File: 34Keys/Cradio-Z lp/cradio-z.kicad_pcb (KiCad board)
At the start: 2 copper layers, 114.1 x 83.1 mm, 22 parts, among them J1 MJ-4PP-9, SW10 SW_PUSH, SW11 SW_PUSH, SW12 SW_PUSH, SW14 SW_PUSH, SW15 SW_PUSH, SW16 SW_PUSH, SW17 SW_PUSH, SW18 SW_PUSH, SW2 SW_PUSH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

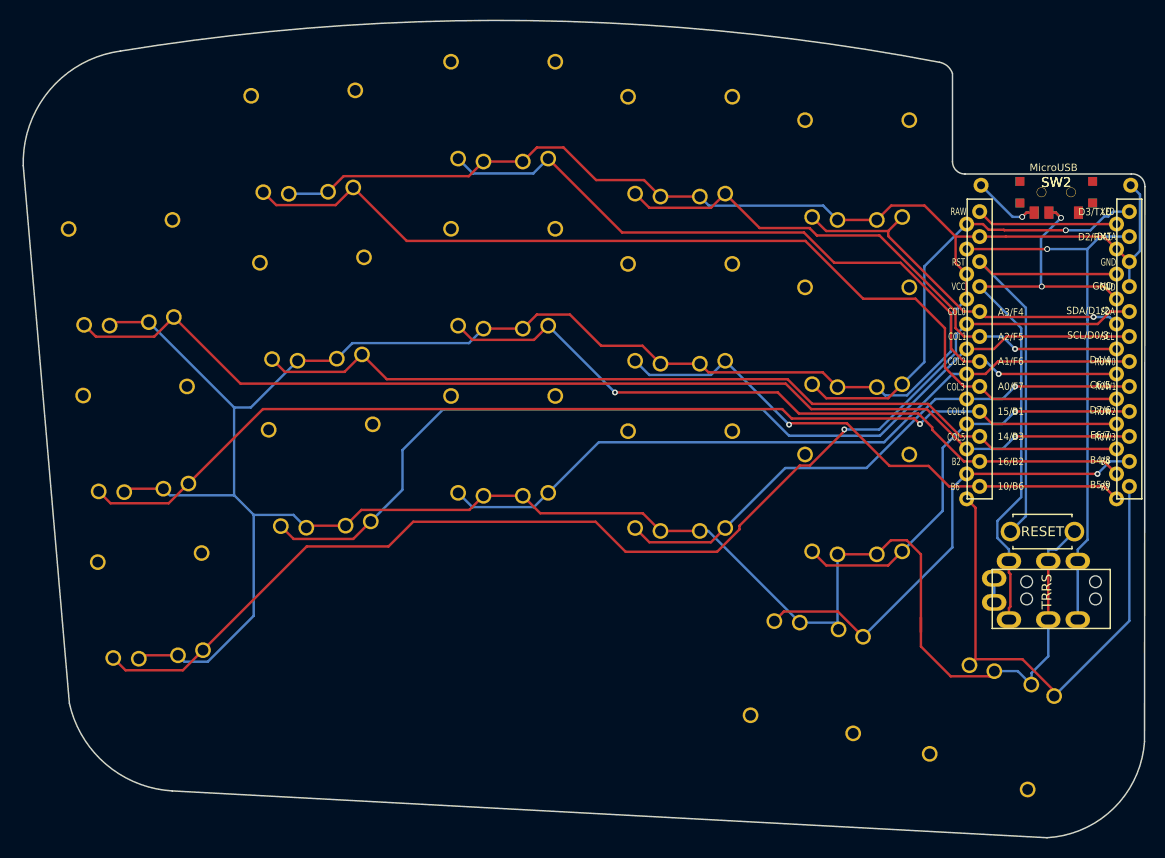
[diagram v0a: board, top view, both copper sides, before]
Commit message: delete somome bits that were really bad or superceded
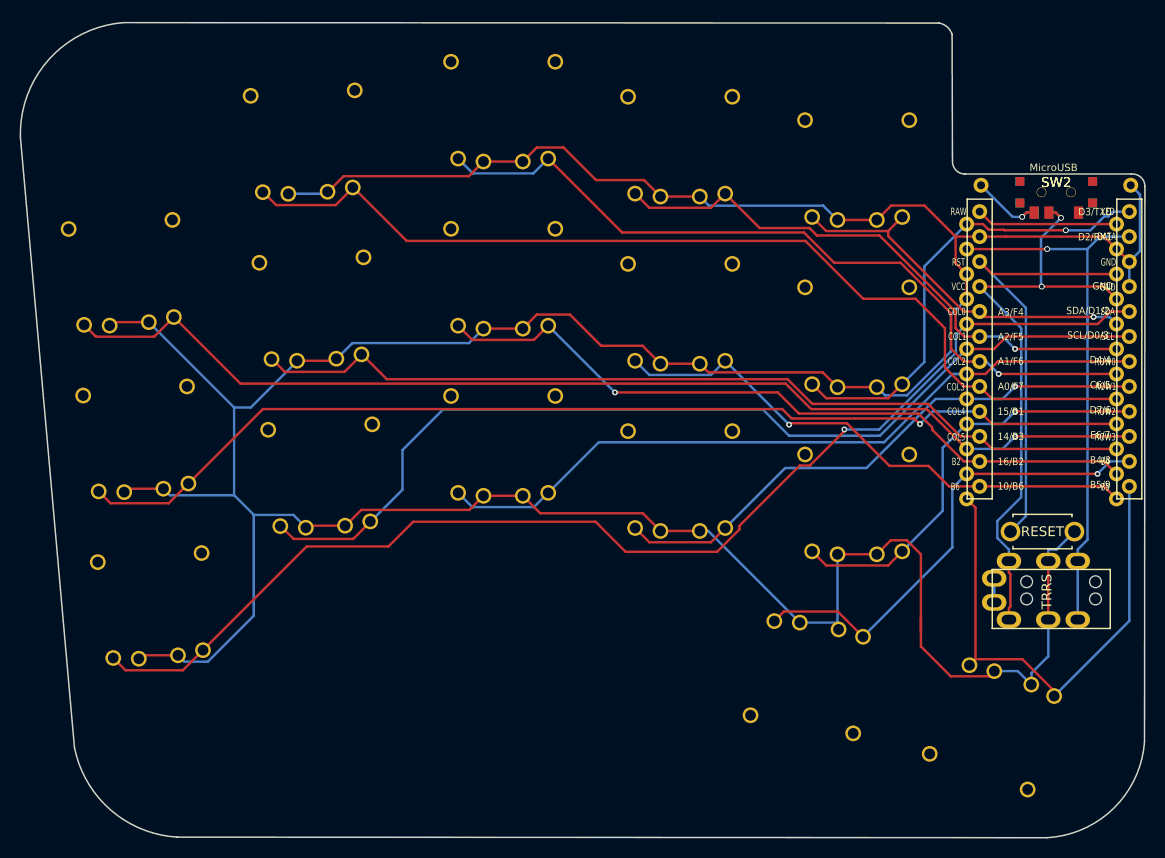
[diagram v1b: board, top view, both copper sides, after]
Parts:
- moved SW15 0.05 mm to (61.6, 62.1)
- moved SW3 0.05 mm to (59.9, 28.2)
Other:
- board size 114.1 x 83.1 mm -> 114.4 x 82.9 mm
